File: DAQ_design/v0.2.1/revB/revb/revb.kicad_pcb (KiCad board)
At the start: 2 copper layers, 19 parts, among them Q1 BC549, Q2 IRF9540N, Q3 IRF540N, Q4 BC549, Q5 IRF9540N, Q6 IRF540N, U1 ADS1115IDGS

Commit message: revb changes
revb changes
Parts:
- moved R1 53.5 mm to (138.0, 64.8)
- moved R2 53.5 mm to (138.0, 69.8)
- moved R3 53.5 mm to (138.0, 74.9)
- moved R4 53.5 mm to (138.0, 80.0)
- moved Screw_Terminal2 37.1 mm to (166.4, 119.4)
- moved Screw_Terminal1 36.1 mm to (142.2, 119.4)
- moved Barrel_Jack1 26.8 mm to (143.2, 55.5), turned to -90 degrees
- moved U1 25.7 mm to (167.6, 92.2)
- moved Q3 22.8 mm to (148.6, 80.0), turned to 180 degrees
- moved Q1 20.8 mm to (144.8, 63.5)
- moved Q2 19.9 mm to (148.6, 71.1), turned to 180 degrees
- moved Arduino1 17.3 mm to (191.8, 83.8), turned to 180 degrees
- moved Q6 15.6 mm to (163.8, 80.0), turned to 180 degrees
- moved Q5 13.7 mm to (163.8, 71.1), turned to 180 degrees
- moved Q4 7.18 mm to (157.5, 63.5)
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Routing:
- added copper zone on B.Cu, net AIN0
- added copper zone on F.Cu, net VPP
- removed copper zone on B.Cu, net (none)
- removed copper zone on F.Cu, net (none)

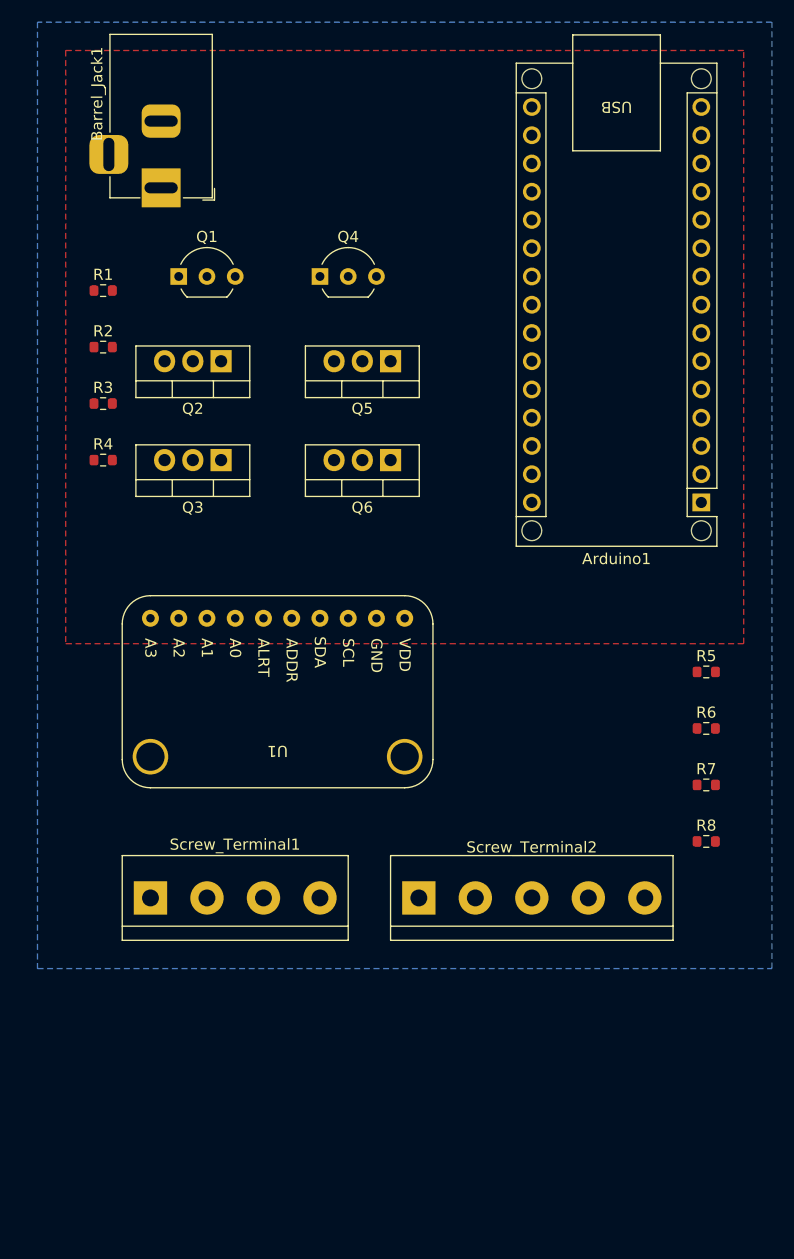
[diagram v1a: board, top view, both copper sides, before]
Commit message: updates to revb
graphics and traces
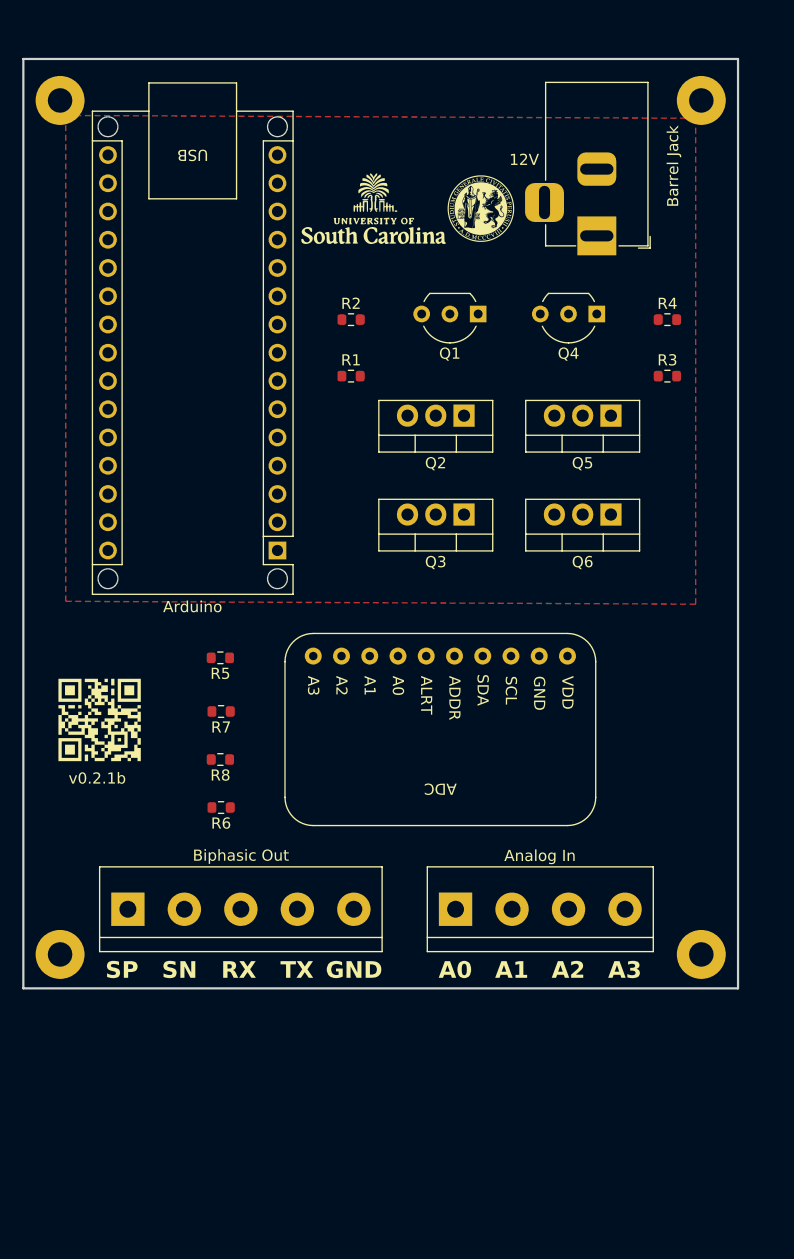
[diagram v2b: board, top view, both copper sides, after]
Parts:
- added G2: LOGO, boardGraphics:uofsc, F.Cu at (162.3, 57.4)
- added G3: LOGO, boardGraphics:upg, F.Cu at (172.0, 57.4)
- added G5: LOGO, boardGraphics:schematic, B.Cu at (165.9, 101.1)
- added G7: LOGO, boardGraphics:github, F.Cu at (137.7, 103.4)
- added REF1: MountingHole_2.2mm_M2_Pad, MountingHole:MountingHole_2.2mm_M2_Pad, F.Cu at (191.8, 124.5)
- added REF2: MountingHole_2.2mm_M2_Pad, MountingHole:MountingHole_2.2mm_M2_Pad, F.Cu at (134.1, 124.5)
- added REF3: MountingHole_2.2mm_M2_Pad, MountingHole:MountingHole_2.2mm_M2_Pad, F.Cu at (134.1, 47.7)
- added REF4: MountingHole_2.2mm_M2_Pad, MountingHole:MountingHole_2.2mm_M2_Pad, F.Cu at (191.8, 47.7)
- Analog In: renamed from Screw_Terminal1
- Barrel Jack: renamed from Barrel_Jack1
- Biphasic Out: renamed from Screw_Terminal2
- moved R4 52.3 mm to (188.7, 67.4)
- moved R3 50.8 mm to (188.7, 72.5)
- moved R8 44.3 mm to (148.5, 106.9), turned to 180 degrees
- moved R6 44.2 mm to (148.6, 111.3), turned to 180 degrees
- moved R7 44.1 mm to (148.6, 102.6), turned to 180 degrees
- moved R5 43.7 mm to (148.5, 97.8), turned to 180 degrees
- moved Barrel Jack 39.4 mm to (182.4, 59.8)
- moved Arduino 38.4 mm to (153.7, 88.1)
- moved Analog In 27.5 mm to (169.7, 120.4)
- moved Q1 27.1 mm to (171.7, 66.9), turned to 180 degrees
- moved Biphasic Out 26.2 mm to (140.2, 120.4)
- moved Q4 25.1 mm to (182.4, 66.9), turned to 180 degrees
- moved R1 23.6 mm to (160.3, 72.5)
- moved R2 22.4 mm to (160.3, 67.4)
- moved Q2 22.4 mm to (170.4, 76.0)
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- renumbered U1 to ADC, Arduino1 to Arduino
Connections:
- Arduino pad 27: unconnected-(Arduino1-+5V-Pad27) -> VDD
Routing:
- removed copper zone on B.Cu, net AIN0
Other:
- board outline added: 64.3 x 83.6 mm
- board text added: "12V"
- board text added: "A0"
- board text added: "A1"
- board text added: "A2"
- board text added: "A3"
- board text added: "GND"
- board text added: "H. B. Birgin, David Wamai, Joud Satme, Austin R. J. Downey"
- board text added: "RX"
- board text added: "SN"
- board text added: "SP"
- board text added: "TX"
- board text added: "v0.2.1b"

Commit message: vias?
VIAS?
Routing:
- net AIN0: track 0.00 -> 182.6 mm, vias 0 -> 4
- net Net-(Arduino1-SCL/A5): track 0.00 -> 95.5 mm
- net Net-(Arduino1-SDA/A4): track 0.00 -> 81.4 mm
- net SP: track 0.00 -> 70.2 mm
- net VDD: track 0.00 -> 67.9 mm, vias 0 -> 1
- net SN: track 0.00 -> 67.0 mm
- net LOGIC1: track 0.00 -> 55.7 mm
- net LOGIC2: track 0.00 -> 55.1 mm
- net RX: track 0.00 -> 37.8 mm
- net VPP: track 0.00 -> 28.8 mm, vias 0 -> 4
- net Net-(Screw_Terminal2-Pin_4): track 0.00 -> 22.8 mm
- net TX: track 0.00 -> 21.3 mm
- net Net-(Q1-C): track 0.00 -> 21.3 mm
- net Net-(Q4-C): track 0.00 -> 17.3 mm
- net Net-(Arduino1-~{RESET}-Pad3): track 0.00 -> 17.3 mm
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- added copper zone on B.Cu, net AIN0

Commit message: storing
storing
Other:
- board text added: "v0.2.1"
- board text removed: "v0.2.1b"
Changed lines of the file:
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@@
     (effects (font (size 1.5 1.5) (thickness 0.3) bold) (justify left bottom))
   )
-  (gr_text "v0.2.1b" (at 134.874 109.22) (layer "F.SilkS")
+  (gr_text "v0.2.1\n" (at 134.874 109.22) (layer "F.SilkS")
     (effects (font (size 1 1) (thickness 0.15)) (justify left bottom))
   )
@@
   )
   (segment (start 169.672 102.806) (end 164.497 97.631) (width 0.25) (layer "F.Cu") (net 1))
-  (segment (start 165.862 94.488) (end 170.143 90.207) (width 0.25) (layer "F.Cu") (net 1))
   (segment (start 171.159 90.207) (end 171.196 90.17) (width 0.25) (layer "F.Cu") (net 1))
   (segment (start 165.862 126.492) (end 163.068 123.698) (width 0.25) (layer "F.Cu") (net 1))
   (segment (start 159.258 81.026) (end 157.48 82.804) (width 0.25) (layer "F.Cu") (net 1))
   (segment (start 179.832 124.206) (end 178.562 125.476) (width 0.25) (layer "F.Cu") (net 1))
-  (segment (start 170.143 90.207) (end 171.159 90.207) (width 0.25) (layer "F.Cu") (net 1))
   (segment (start 159.417 112.935) (end 159.417 97.631) (width 0.25) (layer "F.Cu") (net 1))
   (segment (start 161.798 81.026) (end 159.258 81.026) (width 0.25) (layer "F.Cu") (net 1))
@@
   (segment (start 164.592 123.698) (end 164.592 118.11) (width 0.25) (layer "F.Cu") (net 1))
   (segment (start 174.752 120.396) (end 174.752 123.698) (width 0.25) (layer "F.Cu") (net 1))
+  (segment (start 171.196 90.17) (end 170.18 90.17) (width 0.25) (layer "F.Cu") (net 1))
+  (segment (start 170.18 90.17) (end 165.862 94.488) (width 0.25) (layer "F.Cu") (net 1))
   (segment (start 174.752 123.698) (end 173.99 124.46) (width 0.25) (layer "F.Cu") (net 1))
   (segment (start 173.99 124.46) (end 167.132 124.46) (width 0.25) (layer "F.Cu") (net 1))

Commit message: start on revb fixes
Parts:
- removed ADC: ADS1115IDGS, ads1115module:Adafruit_ADS1115
- removed Analog In: Screw_Terminal_01x04, TerminalBlock:TerminalBlock_bornier-4_P5.08mm
- removed Arduino: Arduino_Nano_Every, Module:Arduino_Nano_WithMountingHoles
- removed Barrel Jack: Barrel_Jack, Connector_BarrelJack:BarrelJack_Horizontal
- removed Biphasic Out: Screw_Terminal_01x05, TerminalBlock:TerminalBlock_bornier-5_P5.08mm
- removed REF1, REF2, REF3, REF4: MountingHole_2.2mm_M2_Pad, MountingHole:MountingHole_2.2mm_M2_Pad
- added Arduino1: Arduino_Nano_Every, Module:Arduino_Nano_WithMountingHoles, F.Cu at (152.4, 88.9)
- added Barrel_Jack1: Barrel_Jack, Connector_BarrelJack:BarrelJack_Horizontal, F.Cu at (182.9, 59.3)
- added Screw_Terminal1: Screw_Terminal_01x04, TerminalBlock:TerminalBlock_bornier-4_P5.08mm, F.Cu at (170.2, 119.4)
- added Screw_Terminal2: Screw_Terminal_01x05, TerminalBlock:TerminalBlock_bornier-5_P5.08mm, F.Cu at (139.7, 119.4)
- added U1: ADS1115IDGS, ads1115module:Adafruit_ADS1115, F.Cu at (190.5, 94.5)
- R1, R2, R3, R4, R5, R6, R7, R8: footprint Resistor_SMD:R_0603_1608Metric -> Resistor_SMD:R_1206_3216Metric
- moved R5 9.02 mm to (154.9, 104.1), turned to 90 degrees
- moved Q1 7.37 mm to (164.3, 66.9), turned to 0 degrees
- moved Q4 7.37 mm to (175.0, 66.9), turned to 0 degrees
- moved R8 4.67 mm to (144.8, 104.1), turned to 90 degrees
- moved R6 3.36 mm to (149.9, 108.1), turned to -90 degrees
- moved Q2 2.79 mm to (167.6, 76.0)
- moved Q3 2.79 mm to (167.6, 84.9)
- moved R1 2.79 mm to (157.5, 72.5)
- moved R2 2.79 mm to (157.5, 67.4)
- moved R3 2.79 mm to (185.9, 72.5)
- moved R4 2.79 mm to (185.9, 67.4)
- moved Q5 2.79 mm to (180.8, 76.0)
- moved Q6 2.79 mm to (180.8, 84.9)
- moved R7 1.67 mm to (149.9, 101.5), turned to 90 degrees
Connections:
- net AIN0 renamed GND
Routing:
- net GND: track 182.7 -> 0.00 mm, vias 4 -> 0
- net Net-(Arduino1-SCL/A5): track 95.5 -> 0.00 mm
- net Net-(Arduino1-SDA/A4): track 81.4 -> 0.00 mm
- net SP: track 70.2 -> 0.00 mm
- net VDD: track 67.9 -> 0.00 mm, vias 1 -> 0
- net SN: track 67.0 -> 0.00 mm
- net LOGIC1: track 55.7 -> 0.00 mm
- net LOGIC2: track 55.1 -> 0.00 mm
- net RX: track 37.8 -> 0.00 mm
- net VPP: track 28.8 -> 0.00 mm, vias 4 -> 0
- net Net-(Screw_Terminal2-Pin_4): track 22.8 -> 0.00 mm
- net TX: track 21.3 -> 0.00 mm
- net Net-(Q1-C): track 21.3 -> 0.00 mm
- net Net-(Q4-C): track 17.3 -> 0.00 mm
- net Net-(Arduino1-~{RESET}-Pad3): track 17.3 -> 0.00 mm
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- added copper zone on B.Cu, net AN0
- removed copper zone on B.Cu, net GND

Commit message: attempted fixes
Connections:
- Screw_Terminal1 pad 1: AN0 -> AIN3
- Screw_Terminal1 pad 2: AIN1 -> AIN2
- Screw_Terminal1 pad 3: AIN2 -> AIN1
- Screw_Terminal1 pad 4: AIN3 -> AN0
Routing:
- removed copper zone on F.Cu, net VPP
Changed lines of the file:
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@@
       (stroke (width 0.1) (type solid)) (layer "F.Fab"))
     (pad "1" thru_hole rect (at 0 0) (size 3 3) (drill 1.52) (layers "*.Cu" "*.Mask")
-      (net 1 "AN0") (pinfunction "Pin_1") (pintype "passive"))
+      (net 39 "AIN3") (pinfunction "Pin_1") (pintype "passive"))
     (pad "2" thru_hole circle (at 5.08 0) (size 3 3) (drill 1.52) (layers "*.Cu" "*.Mask")
-      (net 41 "AIN1") (pinfunction "Pin_2") (pintype "passive"))
+      (net 40 "AIN2") (pinfunction "Pin_2") (pintype "passive"))
     (pad "3" thru_hole circle (at 10.16 0) (size 3 3) (drill 1.52) (layers "*.Cu" "*.Mask")
-      (net 40 "AIN2") (pinfunction "Pin_3") (pintype "passive"))
+      (net 41 "AIN1") (pinfunction "Pin_3") (pintype "passive"))
     (pad "4" thru_hole circle (at 15.24 0) (size 3 3) (drill 1.52) (layers "*.Cu" "*.Mask")
-      (net 39 "AIN3") (pinfunction "Pin_4") (pintype "passive"))
+      (net 1 "AN0") (pinfunction "Pin_4") (pintype "passive"))
     (model "${KICAD6_3DMODEL_DIR}/TerminalBlock.3dshapes/TerminalBlock_bornier-4_P5.08mm.wrl"
       (offset (xyz 7.619999886 0 0))
@@
     (effects (font (size 1.5 1.5) (thickness 0.3) bold) (justify left bottom))
   )
-  (gr_text "A2" (at 178.308 126.746) (layer "F.SilkS")
+  (gr_text "A2" (at 173.228 126.746) (layer "F.SilkS")
     (effects (font (size 1.5 1.5) (thickness 0.3) bold) (justify left bottom))
   )
@@
     (effects (font (size 1.5 1.5) (thickness 0.3) bold) (justify left bottom))
   )
-  (gr_text "A0" (at 168.148 126.746) (layer "F.SilkS")
+  (gr_text "A0" (at 183.388 126.746) (layer "F.SilkS")
     (effects (font (size 1.5 1.5) (thickness 0.3) bold) (justify left bottom))
   )
@@
     (effects (font (size 1.5 1.5) (thickness 0.3) bold) (justify left bottom))
   )
-  (gr_text "A3\n" (at 183.388 126.746) (layer "F.SilkS")
+  (gr_text "A3\n" (at 168.148 126.746) (layer "F.SilkS")
     (effects (font (size 1.5 1.5) (thickness 0.3) bold) (justify left bottom))
   )
-  (gr_text "A1" (at 173.228 126.746) (layer "F.SilkS")
+  (gr_text "A1" (at 178.308 126.746) (layer "F.SilkS")
     (effects (font (size 1.5 1.5) (thickness 0.3) bold) (justify left bottom))
   )
-  (zone (net 27) (net_name "VPP") (layer "F.Cu") (hatch edge 0.5)
-    (connect_pads (clearance 0.5))
-    (min_thickness 0.25) (filled_areas_thickness no)
-    (fill (thermal_gap 0.5) (thermal_bridge_width 0.5) (island_removal_mode 1) (island_area_min 10))
-    (polygon
-      (pts
-        (xy 134.62 49.022)
-        (xy 134.62 92.71)
-        (xy 191.262 92.964)
-        (xy 191.262 49.276)
-      )
-    )
-  )
   (zone (net 1) (net_name "AN0") (layer "B.Cu") (hatch edge 0.5)
